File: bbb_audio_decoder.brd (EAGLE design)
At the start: 110.5 x 100 mm, 180 parts, among them IC1 OPA2134, IC2 LM317, IC3 LM337, IC4 OPA2134, IC5 OPA2134, IC6 OPA2134, P1 PLR135/T9, Q2 BS170, U1 PCM1690, U2 DIR9001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

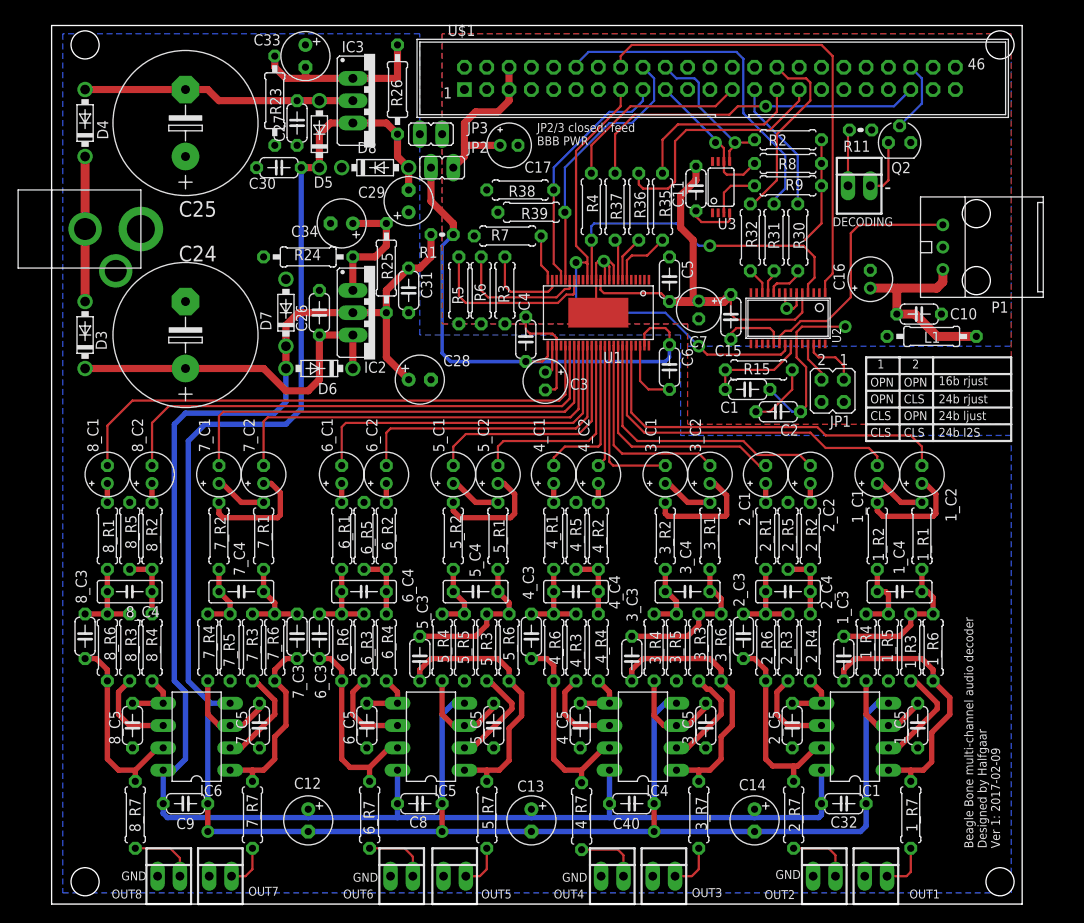
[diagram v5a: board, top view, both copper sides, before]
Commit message: Included LM317 voltage regulator for Beagle Bone
This is the power supply for it, removing the need for a power adapter
for it.

This also changes the AC input to needing a dual winding transformer. My
idea of univeral adapters was nice, until AC "wall warts" became illegal
because of energy laws... Plus, I reduced the supply caps, so I need the
full-wave rectifier now.

I also removed the jumpers to choose to feed the Beagle Bone from the
analog power supply. This was an idea that was never going to work, it
was clear early on. Current demand of one LM317 was too high, and it
would make the analog supply noisy.
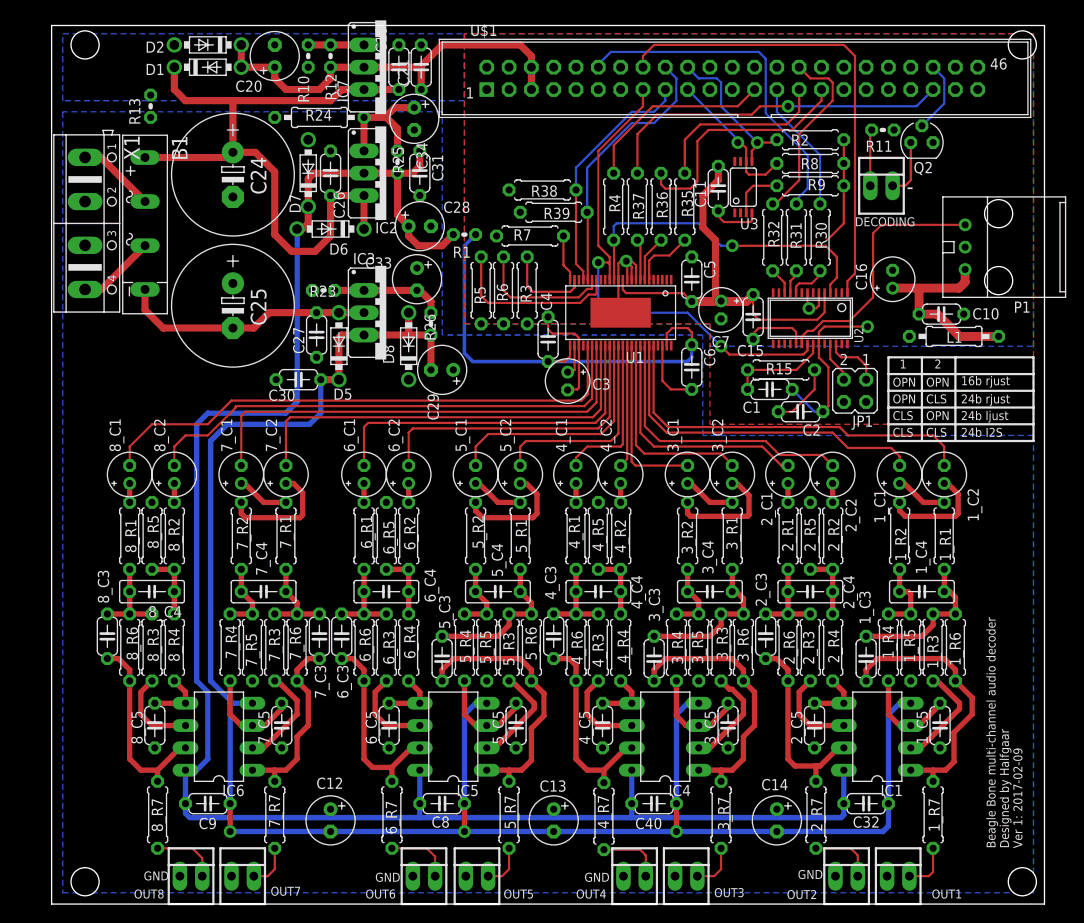
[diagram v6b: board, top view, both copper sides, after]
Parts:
- removed AC: ADAPTER-PLUG-5.5/2.1MM, 0000halfgaar:ADAPTER-PLUG-5.5/2.1MM
- removed C17: 10 µF, rcl:E2-5
- removed D3, D4: 1N4004, diode:DO41-7.6
- removed JP2, JP3: (no value), jumper:JP1
- added B1: (no value), rectifier:FB15
- added C19, C21: 100nF, rcl:C050-024X044
- added C20: 100uF/25V, rcl:E2,5-6
- added D1, D2: 1N4004, diode:DO41-7.6
- added IC7: LM317, v-reg:317TS
- added R10: 715, rcl:0204V
- added R12: 240, rcl:0204V
- added R13: 0, rcl:0204V
- added X1: (no value), con-ptr500:AK500/4
- C24, C25: value 4700uF/25V -> 2200uF/16V; device rcl:E7,5-16 -> rcl:E5-13
- R23, R25, R26: device rcl:0207/10 -> rcl:0204V
- moved C33 28.4 mm to (41.6, 71.1)
- moved R26 26.9 mm to (43.2, 66.0)
- moved C27 24.2 mm to (30.2, 64.8)
- moved C30 24.2 mm to (28.1, 59.7)
- moved D5 24.2 mm to (32.7, 63.5)
- moved IC3 24.2 mm to (38.1, 67.3)
- moved R23 22.3 mm to (31.0, 69.8), turned to 180 degrees
- moved C25 21.5 mm to (20.6, 68.1), turned to 270 degrees
- moved D8 20.7 mm to (40.6, 63.5), turned to 90 degrees
- moved C29 19.6 mm to (44.5, 60.8), turned to 180 degrees
- moved C24 19.0 mm to (20.6, 83.0), turned to 270 degrees
- moved C28 17.5 mm to (41.9, 77.2)
- moved D7 16.1 mm to (29.2, 83.2)
- moved C26 15.9 mm to (31.8, 83.2)
- moved IC2 15.9 mm to (38.1, 83.2)
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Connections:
- new net N$1: B1.AC2, X1.4
- new net N$3: B1.AC1, X1.1
- net AGND: now also R13.1, X1.2, X1.3; no longer AC.3, JP3.2
- net DGND: now also C19.2, C20.-, C21.2, D2.A, R10.1, R13.2; no longer C17.-, JP3.1
- net N$39: now also B1.+, C19.1, D1.C, IC7.3; no longer D3.C
- net N$40: now also IC7.1, R10.2, R12.1; no longer AC.1, D3.A, D4.C
- net N$41: now also B1.-; no longer D4.A
- net VCC: no longer JP2.2
- net VDD_5V: now also C20.+, C21.1, D1.A, D2.C, IC7.2, R12.2; no longer C17.+, JP2.1
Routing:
- net N$39: track 40.9 -> 78.2 mm
- net VDD_5V: track 19.6 -> 47.1 mm
- net V-: track 236.2 -> 213.3 mm
- net V+: track 195.5 -> 208.2 mm
- net N$40: track 16.5 -> 6.35 mm
- net N$3: track 0.00 -> 8.91 mm
- net N$1: track 0.00 -> 8.89 mm
- net VCC: track 60.7 -> 52.0 mm
- net N$42: track 21.0 -> 12.7 mm
- net N$41: track 31.0 -> 28.8 mm
- net VOUT8-: track 59.6 -> 58.1 mm
- net VOUT8+: track 63.7 -> 62.3 mm
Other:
- board size 110.5 x 100 mm -> 113 x 100 mm
- board text removed: "JP2/3 closed: feed BBB PWR"

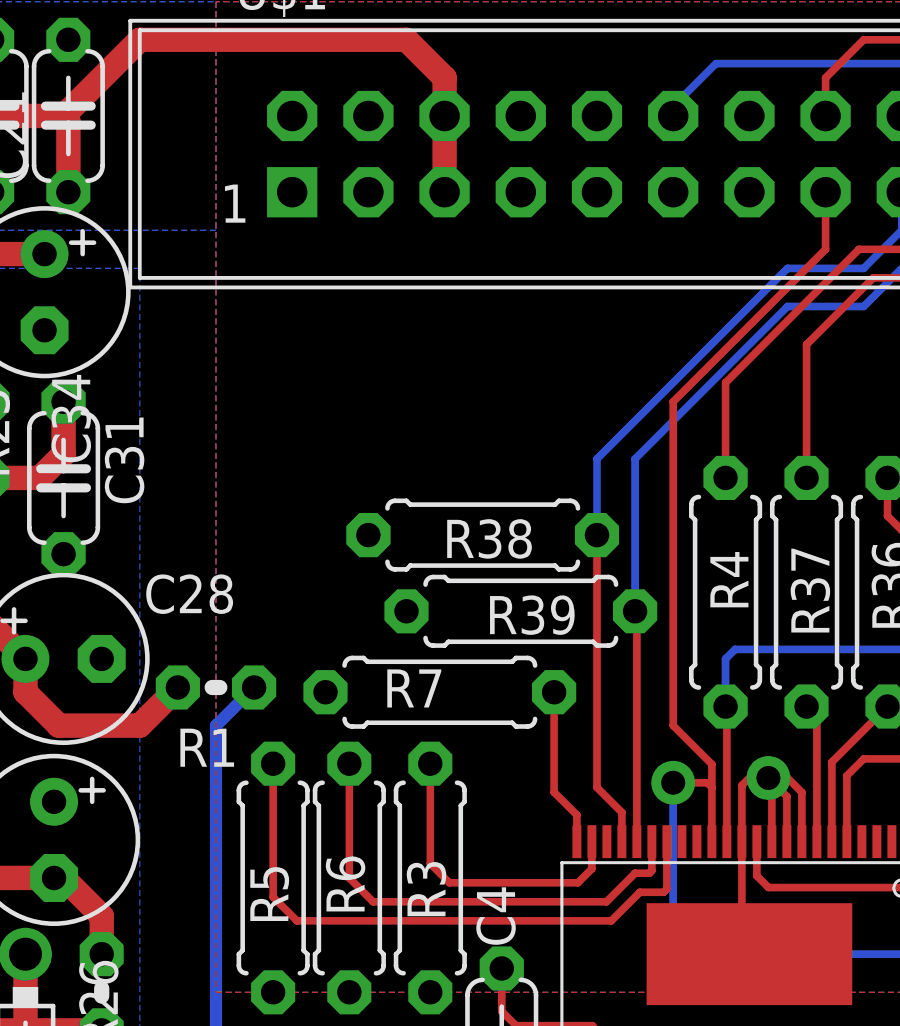
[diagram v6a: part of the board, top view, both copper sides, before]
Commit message: Added molex 22-27-2041 connector for LCD
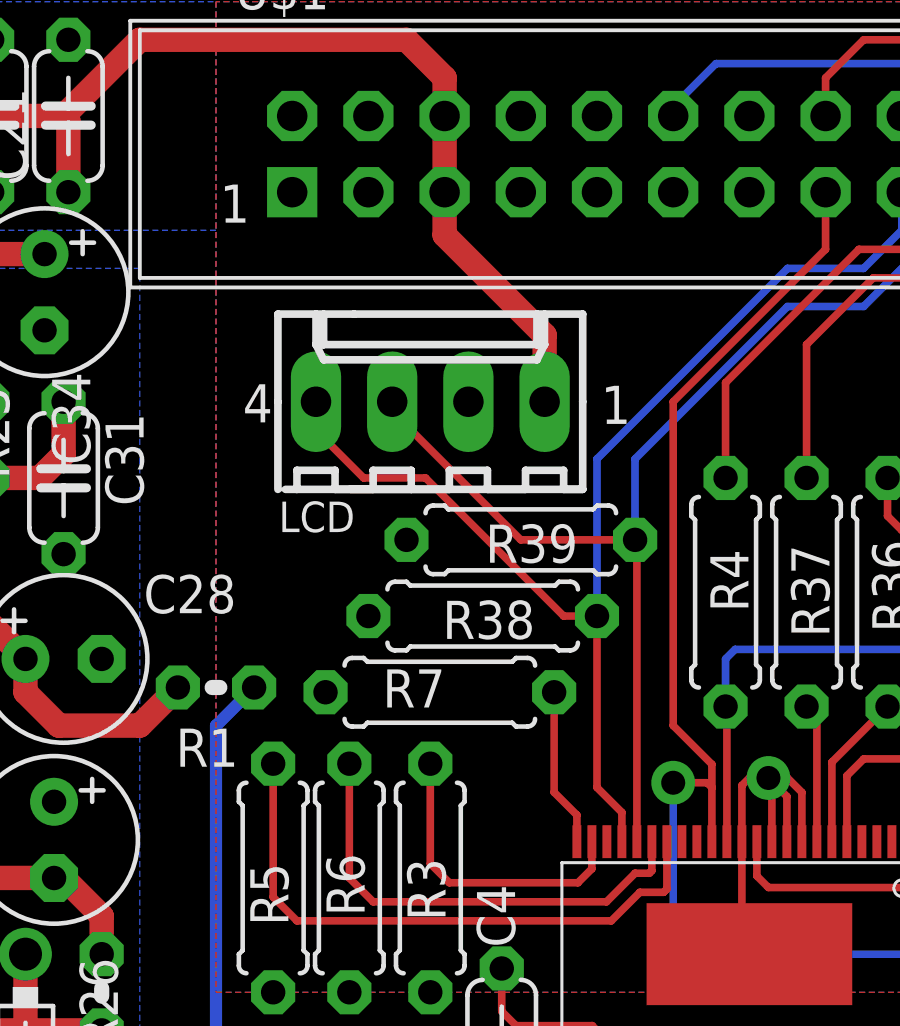
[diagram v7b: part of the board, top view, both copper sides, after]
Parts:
- added LCD: 22-27-2041-04, con-molex:6410-04
- moved R38 2.70 mm to (55.9, 78.6)
- moved R39 2.38 mm to (57.1, 81.1)
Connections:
- net DGND: now also LCD.2
- net SCL: now also LCD.4
- net SDA: now also LCD.3
- net VDD_5V: now also LCD.1
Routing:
- net SCL: track 27.7 -> 40.6 mm
- net SDA: track 30.4 -> 40.6 mm
- net VDD_5V: track 47.1 -> 55.5 mm
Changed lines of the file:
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@@
 <attribute name="VALUE" x="66.1162" y="81.661" size="1.27" layer="27" ratio="10" rot="R270"/>
 </element>
-<element name="R38" library="rcl" package="0207/7" value="5.6k" x="55.88" y="81.28" smashed="yes" rot="R180">
-<attribute name="NAME" x="57.62625" y="81.788" size="1.27" layer="25" ratio="10" rot="R180"/>
-<attribute name="VALUE" x="58.166" y="81.8388" size="1.27" layer="27" ratio="10" rot="R180"/>
-</element>
-<element name="R39" library="rcl" package="0207/7" value="5.6k" x="57.15" y="78.74" smashed="yes" rot="R180">
-<attribute name="NAME" x="59.055" y="79.248" size="1.27" layer="25" ratio="10" rot="R180"/>
-<attribute name="VALUE" x="59.436" y="79.2988" size="1.27" layer="27" ratio="10" rot="R180"/>
+<element name="R38" library="rcl" package="0207/7" value="5.6k" x="55.88" y="78.58125" smashed="yes" rot="R180">
+<attribute name="NAME" x="57.62625" y="79.08925" size="1.27" layer="25" ratio="10" rot="R180"/>
+<attribute name="VALUE" x="58.166" y="79.14005" size="1.27" layer="27" ratio="10" rot="R180"/>
+</element>
+<element name="R39" library="rcl" package="0207/7" value="5.6k" x="57.15" y="81.12125" smashed="yes" rot="R180">
+<attribute name="NAME" x="59.055" y="81.62925" size="1.27" layer="25" ratio="10" rot="R180"/>
+<attribute name="VALUE" x="59.436" y="81.68005" size="1.27" layer="27" ratio="10" rot="R180"/>
 </element>
 <element name="IC4" library="0000halfgaar" package="DIL8" value="OPA2134" x="69.85" y="19.05" rot="R90"/>
@@
 </element>
 <element name="R13" library="rcl" package="0204V" value="0" x="11.27125" y="90.805" rot="R90"/>
+<element name="LCD" library="con-molex" package="6410-04" value="22-27-2041-04" x="54.13375" y="85.725" smashed="yes">
+<attribute name="OC_FARNELL" value="unknown" x="54.13375" y="85.725" size="1.778" layer="27" display="off"/>
+<attribute name="MPN" value="" x="54.13375" y="85.725" size="1.778" layer="27" display="off"/>
+<attribute name="OC_NEWARK" value="unknown" x="54.13375" y="85.725" size="1.778" layer="27" display="off"/>
+<attribute name="MF" value="" x="54.13375" y="85.725" size="1.778" layer="27" display="off"/>
+<attribute name="NAME" x="49.08065" y="81.3801" size="1.016" layer="25" ratio="10"/>
+<attribute name="VALUE" x="49.08065" y="81.1261" size="0.8128" layer="27" ratio="10"/>
+</element>
 </elements>
 <signals>
@@
 <contactref element="R13" pad="2"/>
 <contactref element="C21" pad="2"/>
+<contactref element="LCD" pad="2"/>
 </signal>
 <signal name="AGND">
@@
 <contactref element="U1" pad="21"/>
 <contactref element="R38" pad="1"/>
-<wire x1="59.69" y1="81.28" x2="59.69" y2="83.82" width="0.254" layer="16"/>
+<wire x1="59.69" y1="78.58125" x2="59.69" y2="83.82" width="0.254" layer="16"/>
 <wire x1="59.69" y1="83.82" x2="66.04" y2="90.17" width="0.254" layer="16"/>
 <wire x1="66.04" y1="90.17" x2="68.58" y2="90.17" width="0.254" layer="16"/>
@@
 <wire x1="60.52" y1="71.06" x2="60.52" y2="72.03625" width="0.254" layer="1"/>
 <wire x1="60.52" y1="72.03625" x2="59.69" y2="72.86625" width="0.254" layer="1"/>
-<wire x1="59.69" y1="72.86625" x2="59.69" y2="81.28" width="0.254" layer="1"/>
+<wire x1="59.69" y1="72.86625" x2="59.69" y2="78.58125" width="0.254" layer="1"/>
 <contactref element="U$1" pad="17"/>
 <wire x1="69.85" y1="91.44" x2="69.85" y2="92.71" width="0.254" layer="16"/>
+<contactref element="LCD" pad="4"/>
+<wire x1="50.32375" y1="85.725" x2="50.32375" y2="84.7725" width="0.254" layer="1"/>
+<wire x1="50.32375" y1="84.7725" x2="51.91125" y2="83.185" width="0.254" layer="1"/>
+<wire x1="51.91125" y1="83.185" x2="53.975" y2="83.185" width="0.254" layer="1"/>
+<wire x1="53.975" y1="83.185" x2="58.57875" y2="78.58125" width="0.254" layer="1"/>
+<wire x1="58.57875" y1="78.58125" x2="59.69" y2="78.58125" width="0.254" layer="1"/>
 </signal>
 <signal name="SDA">
@@
 <wire x1="68.58" y1="88.9" x2="66.04" y2="88.9" width="0.254" layer="16"/>
 <wire x1="66.04" y1="88.9" x2="60.96" y2="83.82" width="0.254" layer="16"/>
-<wire x1="60.96" y1="83.82" x2="60.96" y2="78.74" width="0.254" layer="16"/>
-<wire x1="61.02" y1="71.06" x2="61.02" y2="78.68" width="0.254" layer="1"/>
-<wire x1="61.02" y1="78.68" x2="60.96" y2="78.74" width="0.254" layer="1"/>
+<wire x1="60.96" y1="83.82" x2="60.96" y2="81.12125" width="0.254" layer="16"/>
 <contactref element="U$1" pad="18"/>
 <wire x1="71.12" y1="93.98" x2="69.85" y2="95.25" width="0.254" layer="16"/>
+<contactref element="LCD" pad="3"/>
+<wire x1="52.86375" y1="85.725" x2="52.86375" y2="85.4075" width="0.254" layer="1"/>
+<wire x1="52.86375" y1="85.4075" x2="57.15" y2="81.12125" width="0.254" layer="1"/>
+<wire x1="57.15" y1="81.12125" x2="60.96" y2="81.12125" width="0.254" layer="1"/>
+<wire x1="61.02" y1="71.06" x2="61.02" y2="81.06125" width="0.254" layer="1"/>
+<wire x1="61.02" y1="81.06125" x2="60.96" y2="81.12125" width="0.254" layer="1"/>
 </signal>
 <signal name="N$13">
@@
 <wire x1="21.59" y1="95.25" x2="25.4" y2="95.25" width="0.8128" layer="1"/>
 <wire x1="31.75" y1="95.25" x2="35.56" y2="95.25" width="0.8128" layer="1"/>
+<contactref element="LCD" pad="1"/>
+<wire x1="54.61" y1="92.71" x2="54.61" y2="91.28125" width="0.8128" layer="1"/>
+<wire x1="54.61" y1="91.28125" x2="57.94375" y2="87.9475" width="0.8128" layer="1"/>
+<wire x1="57.94375" y1="87.9475" x2="57.94375" y2="85.725" width="0.8128" layer="1"/>
 </signal>
 <signal name="N$1">
